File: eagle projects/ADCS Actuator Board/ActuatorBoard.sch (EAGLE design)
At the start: 278 parts, among them J19 TE_1-84953-1, J20 TE_1-84953-1, J21 TE_1-84953-1, U1 TVS991, U10 DRV10970_MOTOR_DRIVERDRV10970, U12 DRV10970_MOTOR_DRIVERDRV10970, U13 ADS7841E_2K5, U15 TLV9051IDCKR, U19 TLV9051IDCKR, U2 ADS7841E_2K5, U21 TLV9051IDCKR, U23 TLV9051IDCKR, U24 TLV9051IDCKR, U25 ADS7841E_2K5, U26 TLV9051IDCKR, U27 ADS7841E_2K5, U28 TLV9051IDCKR, U29 TLV9051IDCKR, U3 ADS7841E_2K5, U30 TLV9051IDCKR, U31 TLV9051IDCKR, U32 TLV9051IDCKR, U35 BD6210F-E2, U39 BD6210F-E2, U4 ADS7841E_2K5, U5 TVS991, U6 TLV9051IDCKR, U7 DRV10970_MOTOR_DRIVERDRV10970, U8 TVS991, U9 BD6210F-E2

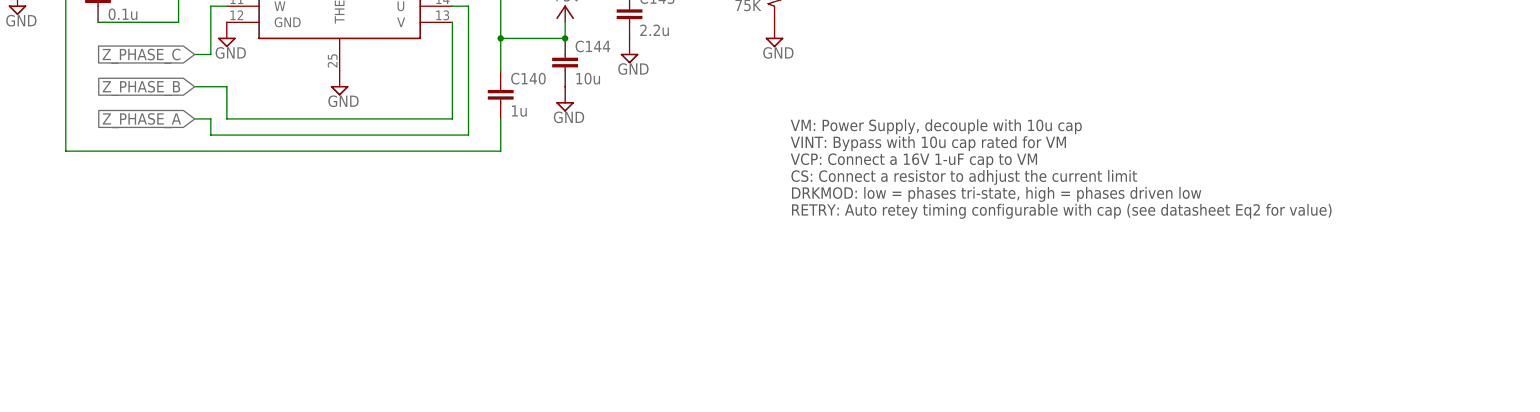
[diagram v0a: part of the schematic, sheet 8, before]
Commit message: Schematic notes edit
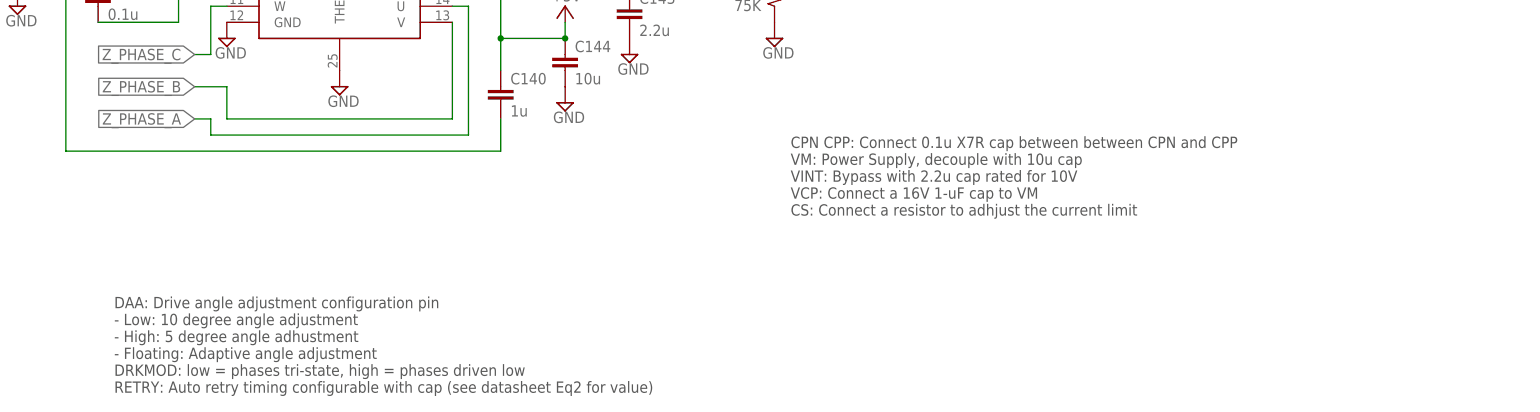
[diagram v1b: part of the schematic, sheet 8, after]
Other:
- note added: "CPN CPP: Connect 0.1u X7R cap between between CPN and CPP VM: Power Supply, decouple with 10u cap VINT: Bypass with 2.2u cap rated for 10V VCP: Connect a 16V 1-uF cap to VM CS: Connect a resistor to adhjust the current limit"
- note added: "DAA: Drive angle adjustment configuration pin - Low: 10 degree angle adjustment - High: 5 degree angle adhustment - Floating: Adaptive angle adjustment DRKMOD: low = phases tri-state, high = phases driven low RETRY: Auto retry timing configurable with cap (see datasheet Eq2 for value)"
- note removed: "VM: Power Supply, decouple with 10u cap VINT: Bypass with 10u cap rated for VM VCP: Connect a 16V 1-uF cap to VM CS: Connect a resistor to adhjust the current limit DRKMOD: low = phases tri-state, high = phases driven low RETRY: Auto retey timing configurable with cap (see datasheet Eq2 for value)"
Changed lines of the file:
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@@
 <setting verticaltext="up"/>
 </settings>
-<grid distance="0.1" unitdist="inch" unit="inch" style="lines" multiple="1" display="no" altdistance="0.05" altunitdist="inch" altunit="inch"/>
+<grid distance="0.1" unitdist="inch" unit="inch" style="lines" multiple="1" display="no" altdistance="0.01" altunitdist="inch" altunit="inch"/>
 <layers>
 <layer number="1" name="Top" color="4" fill="1" visible="no" active="no"/>
@@
 <sheet>
 <plain>
-<text x="177.8" y="43.18" size="1.778" layer="97">VM: Power Supply, decouple with 10u cap
-VINT: Bypass with 10u cap rated for VM
+<text x="177.8" y="43.18" size="1.778" layer="97">CPN CPP: Connect 0.1u X7R cap between between CPN and CPP
+VM: Power Supply, decouple with 10u cap
+VINT: Bypass with 2.2u cap rated for 10V
 VCP: Connect a 16V 1-uF cap to VM
-CS: Connect a resistor to adhjust the current limit
-DRKMOD: low = phases tri-state, high = phases driven low
-RETRY: Auto retey timing configurable with cap (see datasheet Eq2 for value)</text>
+CS: Connect a resistor to adhjust the current limit</text>
 <text x="88.9" y="177.8" size="1.778" layer="97" rot="MR0">NC</text>
 <text x="124.46" y="167.64" size="1.778" layer="97">NC</text>
 <text x="88.9" y="101.6" size="1.778" layer="97" rot="MR0">NC</text>
 <text x="124.46" y="91.44" size="1.778" layer="97">NC</text>
+<text x="71.12" y="15.24" size="1.778" layer="97">DAA: Drive angle adjustment configuration pin
+- Low: 10 degree angle adjustment
+- High: 5 degree angle adhustment
+- Floating: Adaptive angle adjustment
+DRKMOD: low = phases tri-state, high = phases driven low
+RETRY: Auto retry timing configurable with cap (see datasheet Eq2 for value)</text>
 </plain>
 <instances>

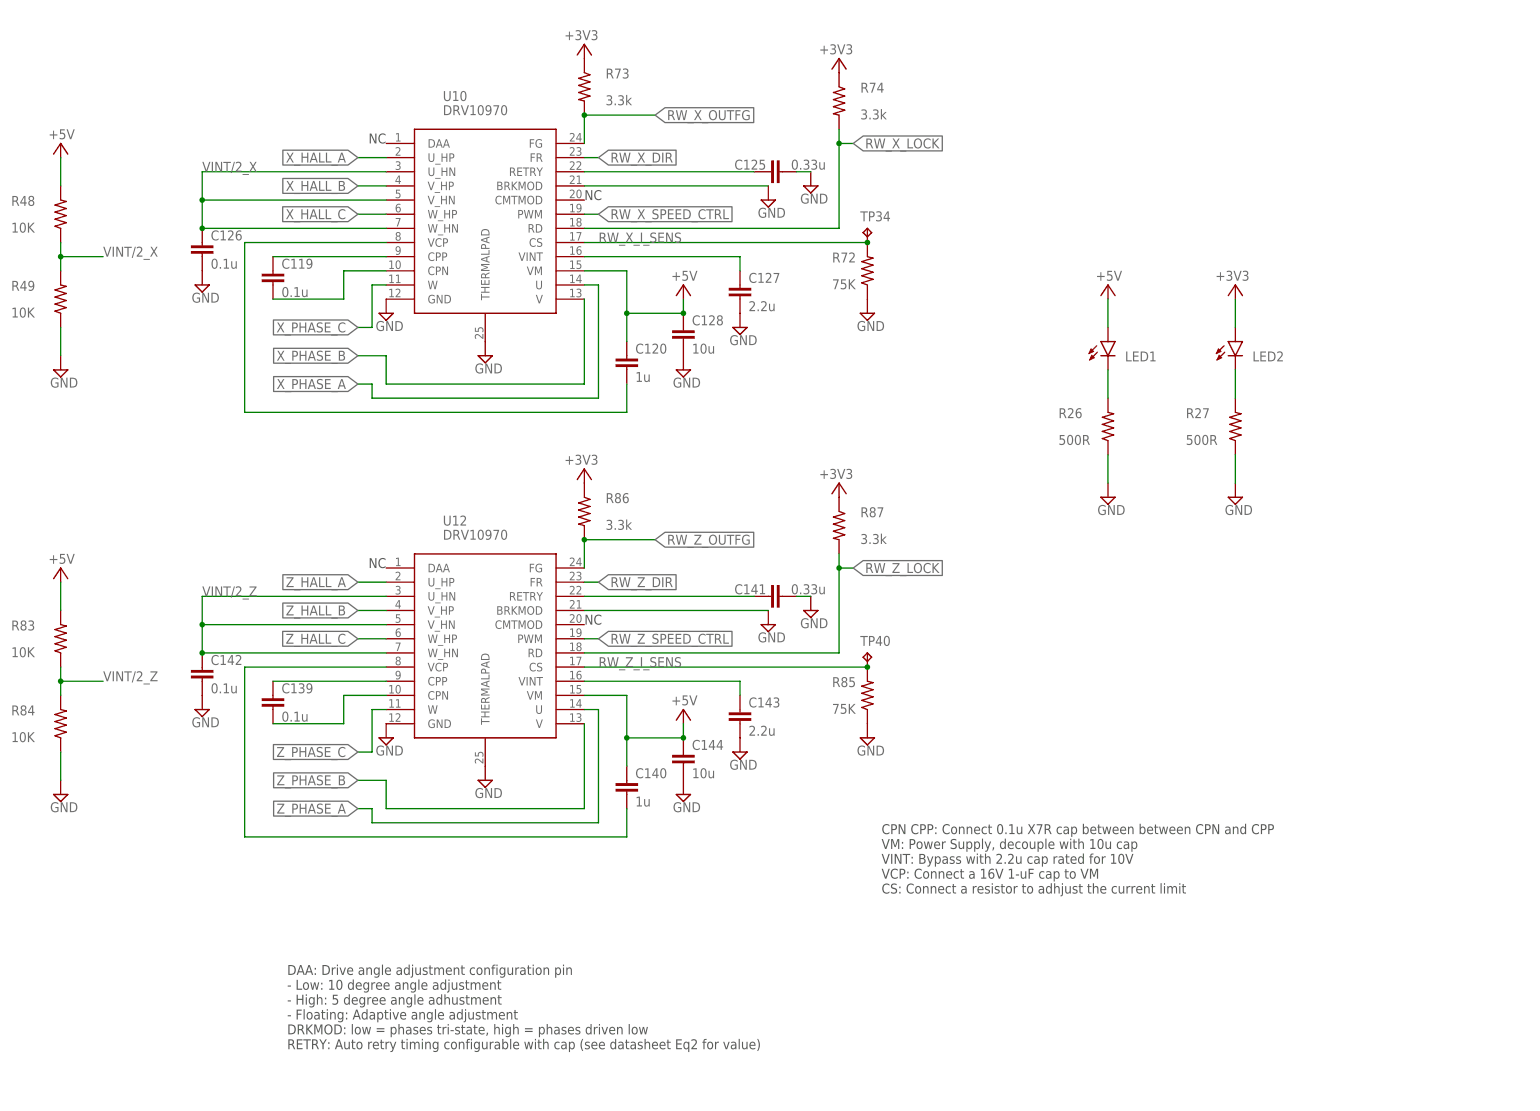
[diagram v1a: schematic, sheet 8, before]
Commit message: Added jumpers for selecting motor break mode
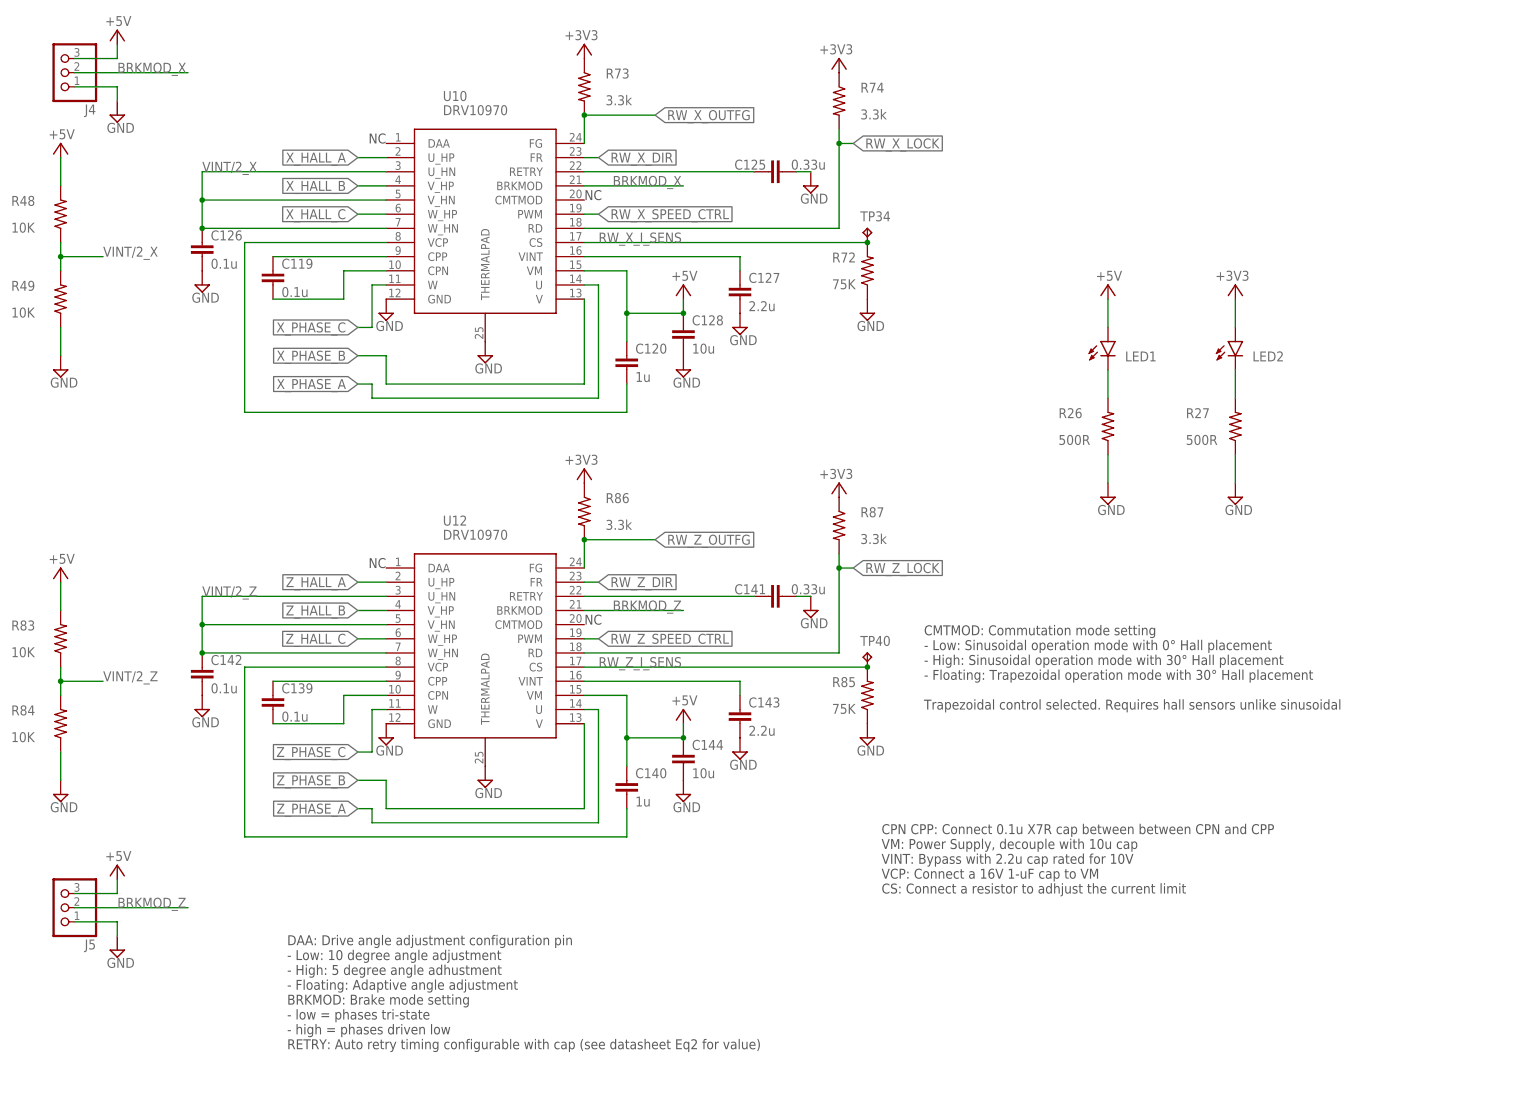
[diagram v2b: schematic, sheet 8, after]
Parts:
- added J4, J5, J6: (no value), my_library:PINHD-1X3
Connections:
- new net BRKMOD_X: J4.2, U10.BRKMOD
- new net BRKMOD_Y: J6.2, U7.BRKMOD
- new net BRKMOD_Z: J5.2, U12.BRKMOD
- net +5V: now also J4.3, J5.3, J6.3
- net GND: now also J4.1, J5.1, J6.1; no longer U10.BRKMOD, U12.BRKMOD, U7.BRKMOD
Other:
- note added: "CMTMOD: Commutation mode setting - Low: Sinusoidal operation mode with 0° Hall placement - High: Sinusoidal operation mode with 30° Hall placement - Floating: Trapezoidal operation mode with 30° Hall placement Trapezoidal control selected. Requires hall sensors unlike sinusoidal"
- note added: "DAA: Drive angle adjustment configuration pin - Low: 10 degree angle adjustment - High: 5 degree angle adhustment - Floating: Adaptive angle adjustment BRKMOD: Brake mode setting - low = phases tri-state - high = phases driven low RETRY: Auto retry timing configurable with cap (see datasheet Eq2 for value)"
- note removed: "DAA: Drive angle adjustment configuration pin - Low: 10 degree angle adjustment - High: 5 degree angle adhustment - Floating: Adaptive angle adjustment DRKMOD: low = phases tri-state, high = phases driven low RETRY: Auto retry timing configurable with cap (see datasheet Eq2 for value)"

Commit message: DONE THIS MFER
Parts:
- added R1, R10, R11, R12, R15, R2, R7, R8, R9: 4.7k, rcl:R-US_R0402
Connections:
- net +5V: now also R1.2, R10.2, R11.2, R12.2, R15.2, R2.2, R7.2, R8.2, R9.2
- net X_HALL_A: now also R2.1
- net X_HALL_B: now also R1.1
- net X_HALL_C: now also R7.1
- net Y_HALL_A: now also R9.1
- net Y_HALL_B: now also R8.1
- net Y_HALL_C: now also R10.1
- net Z_HALL_A: now also R12.1
- net Z_HALL_B: now also R11.1
- net Z_HALL_C: now also R15.1
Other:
- moved on the sheet: J19, J20, J21, TP2, TP21, TP22, TP23, TP24, TP25, TP4, TP5, TP7

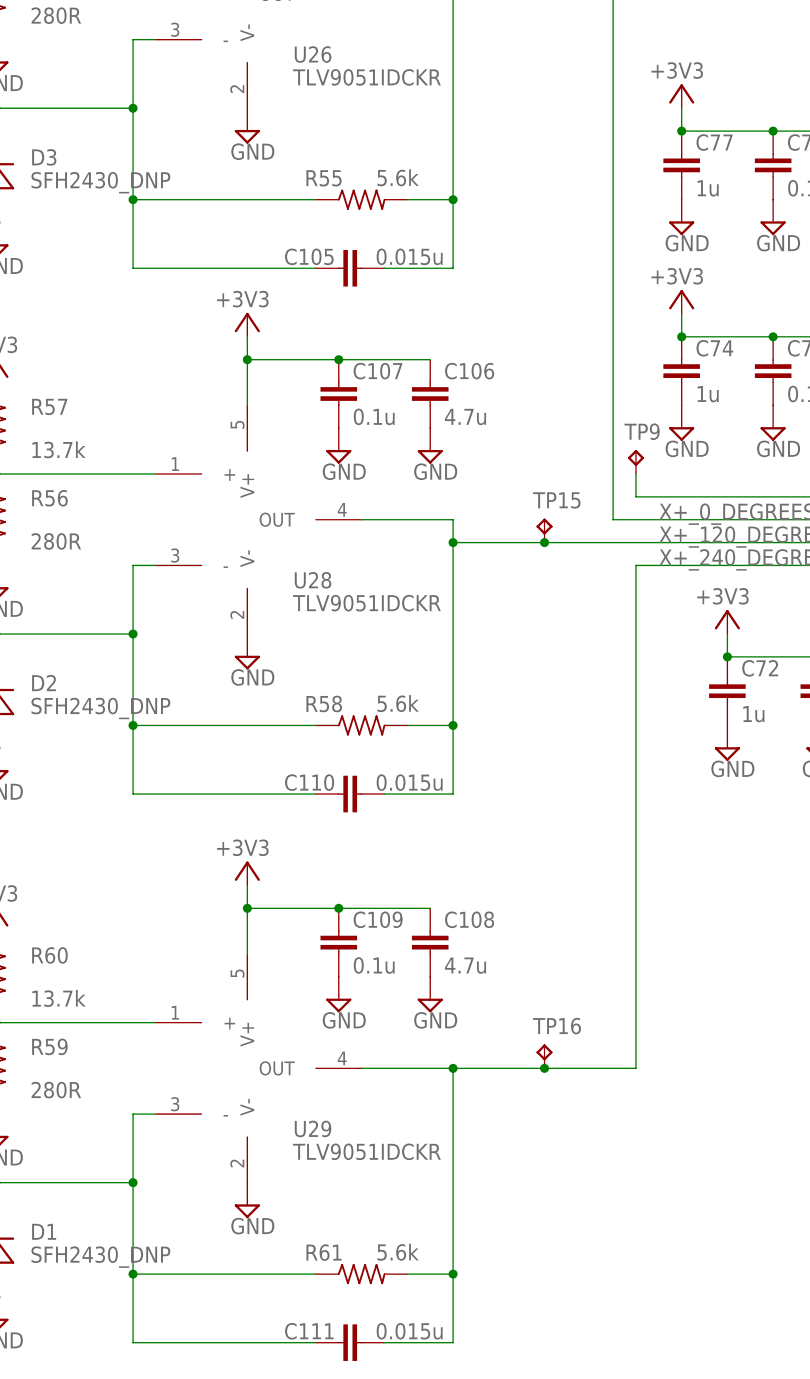
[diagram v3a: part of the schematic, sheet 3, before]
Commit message: changed values for resistance of sun sensor amp
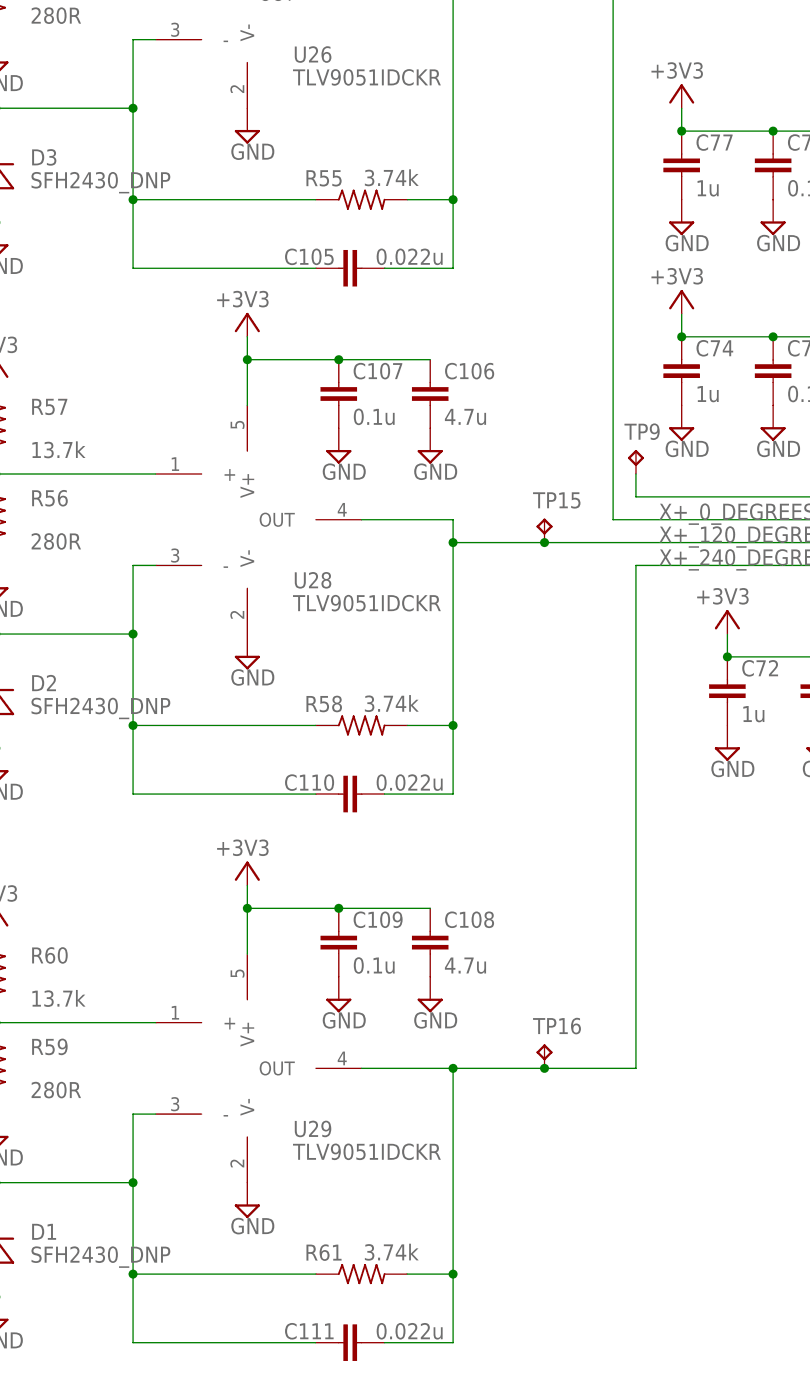
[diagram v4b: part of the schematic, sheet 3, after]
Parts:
- C100, C101, C105, C110, C111, C115, C116, C54, C70, C71, C84, C98: value 0.015u -> 0.022u
- R24, R31, R34, R40, R46, R52, R55, R58, R61, R64, R67, R70: value 5.6k -> 3.74k

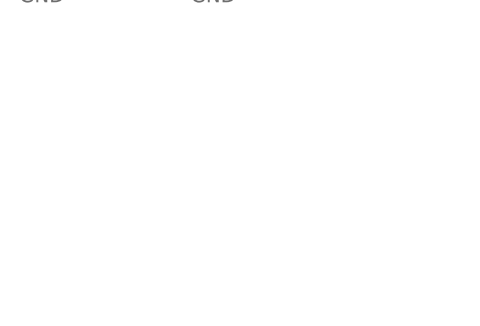
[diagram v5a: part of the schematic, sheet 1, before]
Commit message: Added bom file and rev # to schematic
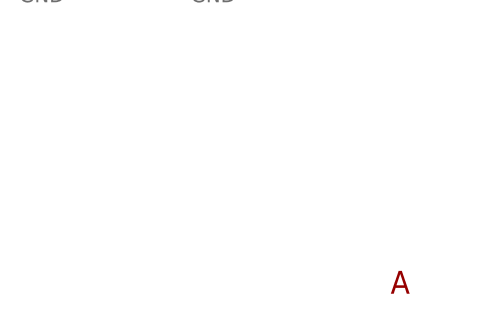
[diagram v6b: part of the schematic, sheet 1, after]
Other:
- note added: "A"
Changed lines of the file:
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@@
  the value of current through the coil scaled by Rcoil/(Rcoil +
  R35)</text>
+<text x="261.62" y="7.62" size="2.54" layer="94">A</text>
 </plain>
 <instances>
@@
 <sheet>
 <plain>
+<text x="261.62" y="7.62" size="2.54" layer="94">A</text>
 </plain>
 <instances>
@@
 <sheet>
 <plain>
+<text x="261.62" y="7.62" size="2.54" layer="94">A</text>
 </plain>
 <instances>
@@
 <sheet>
 <plain>
+<text x="261.62" y="7.62" size="2.54" layer="94">A</text>
 </plain>
 <instances>
@@
 <sheet>
 <plain>
+<text x="261.62" y="7.62" size="2.54" layer="94">A</text>
 </plain>
 <instances>
@@
 <sheet>
 <plain>
+<text x="261.62" y="7.62" size="2.54" layer="94">A</text>
 </plain>
 <instances>
@@
 <text x="76.2" y="63.5" size="1.778" layer="97" rot="MR0">NC</text>
 <text x="111.76" y="53.34" size="1.778" layer="97">NC</text>
+<text x="261.62" y="7.62" size="2.54" layer="94">A</text>
 </plain>
 <instances>
@@
 - Floating: Trapezoidal operation mode with 30° Hall placement
 Trapezoidal control selected. Requires hall sensors unlike sinusoidal</text>
+<text x="261.62" y="7.62" size="2.54" layer="94">A</text>
 </plain>
 <instances>
